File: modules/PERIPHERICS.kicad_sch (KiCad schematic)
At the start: 6 parts, among them J1 Conn_01x04, J2 Conn_01x04

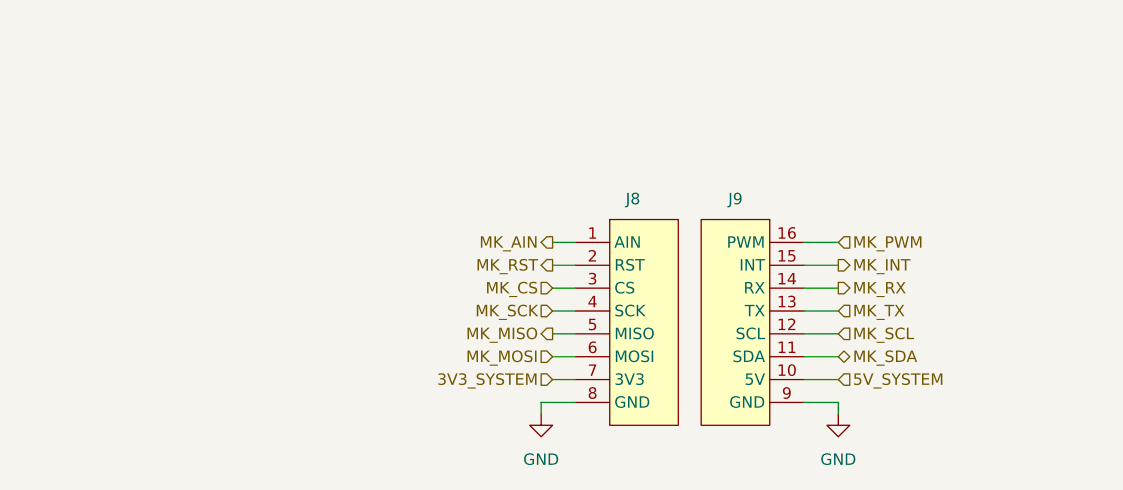
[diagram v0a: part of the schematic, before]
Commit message: correction of mikroBUS, USB on ESP32 and power mosfet
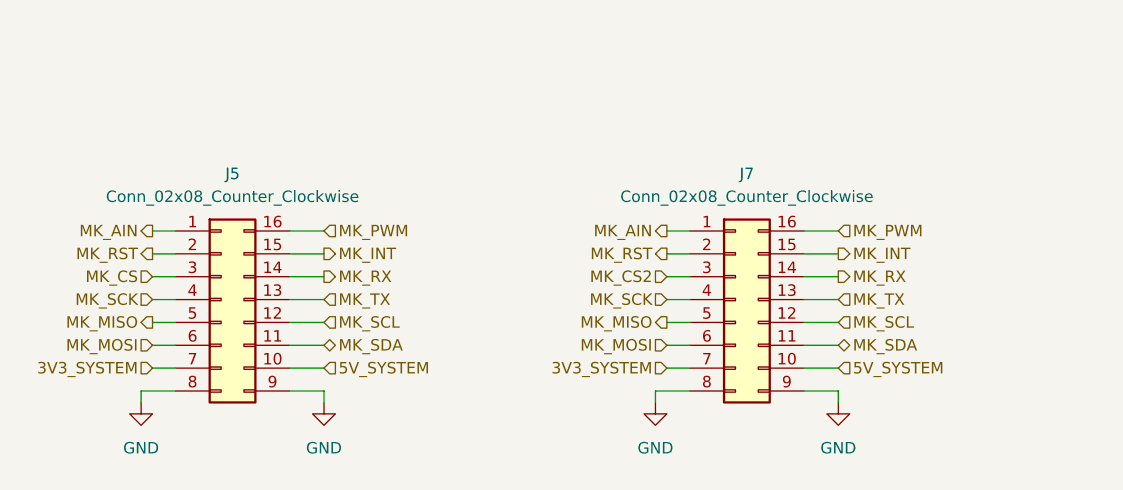
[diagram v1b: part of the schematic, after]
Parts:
- removed J8: ~, Sadman_connectors:MikroBUS_Left, symbol Sadman_connnector:MikroBUS_Left
- removed J9: ~, Sadman_connectors:MikroBUS_Right, symbol Sadman_connnector:MikroBUS_Right
- added J5, J7: Conn_02x08_Counter_Clockwise, Sadman_connectors:CONN2X8_MIKROE-4248_MKE, symbol Connector_Generic:Conn_02x08_Counter_Clockwise
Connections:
- net 3V3_SYSTEM: now also J5.7 (Pin_7), J7.7 (Pin_7)
- net 5V_SYSTEM: now also J5.10 (Pin_10), J7.10 (Pin_10)
- net GND: now also J5.8 (Pin_8), J5.9 (Pin_9), J7.8 (Pin_8), J7.9 (Pin_9)
- net MK_AIN: now also J5.1 (Pin_1), J7.1 (Pin_1)
- net MK_CS: now also J5.3 (Pin_3)
- net MK_INT: now also J5.15 (Pin_15), J7.15 (Pin_15)
- net MK_MISO: now also J5.5 (Pin_5), J7.5 (Pin_5)
- net MK_MOSI: now also J5.6 (Pin_6), J7.6 (Pin_6)
- net MK_PWM: now also J5.16 (Pin_16), J7.16 (Pin_16)
- net MK_RST: now also J5.2 (Pin_2), J7.2 (Pin_2)
- net MK_RX: now also J5.14 (Pin_14), J7.14 (Pin_14)
- net MK_SCK: now also J5.4 (Pin_4), J7.4 (Pin_4)
- net MK_SCL: now also J5.12 (Pin_12), J7.12 (Pin_12)
- net MK_SDA: now also J5.11 (Pin_11), J7.11 (Pin_11)
- net MK_TX: now also J5.13 (Pin_13), J7.13 (Pin_13)
- new net MK_CS2: J7.3 (Pin_3)

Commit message: save
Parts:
- added TP12, TP13, TP14, TP15, TP16, TP17: TestPoint, TestPoint:TestPoint_THTPad_D1.0mm_Drill0.5mm, symbol Connector:TestPoint
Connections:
- net MK_AIN: now also TP12.1
- net MK_CS: now also TP14.1
- net MK_MISO: now also TP16.1
- net MK_MOSI: now also TP17.1
- net MK_RST: now also TP13.1
- net MK_SCK: now also TP15.1

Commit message: Cambio de layout, correccion de pinout
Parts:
- removed C22, C23: 100nF, Capacitor_SMD:C_0402_1005Metric, symbol Device:C
- added TP19, TP20, TP26, TP27, TP28, TP29, TP30, TP31, TP32, TP33, TP9: TestPoint, Sadman_TP:TP_2.8mm_1mm, symbol Connector:TestPoint
- TP12, TP13, TP14, TP15, TP16, TP17: footprint TestPoint:TestPoint_THTPad_D1.0mm_Drill0.5mm -> Sadman_TP:TP_2.8mm_1mm
- renumbered J5 to J2, J7 to J5, J2 to J7
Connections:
- net RP_CLK is gone; now on net MK_SCL: J1.4 (Pin_4), J7.4 (Pin_4)
- net RP_SDA is gone; now on net MK_SDA: J1.3 (Pin_3), J7.3 (Pin_3)
- net MK_AIN: now also TP9.1; no longer J5.1 (Pin_1), TP12.1
- net MK_CS2: now also TP33.1
- net MK_INT: now also TP20.1; no longer J5.15 (Pin_15)
- net MK_MOSI: now also TP15.1; no longer TP17.1
- net MK_PWM: now also TP19.1; no longer J5.16 (Pin_16)
- net MK_RST: now also TP12.1; no longer J5.2 (Pin_2), TP13.1
- net MK_RX: now also TP32.1; no longer J5.14 (Pin_14)
- net MK_SCK: now also TP14.1; no longer TP15.1
- net MK_TX: now also TP31.1; no longer J5.13 (Pin_13)
- net MK_CS renamed MK_CS1
- net MK_CS1: now also TP13.1; no longer TP14.1
- new net MK_AIN2: J5.1 (Pin_1), TP17.1
- new net MK_INT2: J5.15 (Pin_15), TP29.1
- new net MK_PWM2: J5.16 (Pin_16), TP30.1
- new net MK_RST2: J5.2 (Pin_2), TP26.1
- new net MK_RX2: J5.14 (Pin_14), TP28.1
- new net MK_TX2: J5.13 (Pin_13), TP27.1
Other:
- moved on the sheet: J1, J2, J5, J7

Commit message: finishing version 1.0
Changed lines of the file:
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@@
 	(wire
 		(pts
-			(xy 226.6538 119.38) (xy 229.87 119.38)
+			(xy 223.52 119.38) (xy 229.87 119.38)
 		)
 		(stroke
@@
 	(hierarchical_label "MK_RST2"
 		(shape output)
-		(at 226.6538 119.38 180)
-		(effects
-			(font
+		(at 223.52 119.38 180)
+		(effects
+			(font
